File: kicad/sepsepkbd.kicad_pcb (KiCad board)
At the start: 2 copper layers, 170.7 x 127.7 mm, 53 parts, among them J1 MJ-4PP-9, J2 MJ-4PP-9, J3 Conn_01x10_Pin, J4 Conn_01x10_Pin, J5 Conn_01x10_Pin, J6 Conn_01x08_Pin, J7 Conn_01x08_Pin, SW1 SW_PUSH, SW10 SW_PUSH, SW11 SW_PUSH, SW12 SW_PUSH, SW13 SW_PUSH, SW14 SW_PUSH, SW15 SW_PUSH, SW16 SW_PUSH, SW17 SW_PUSH, SW18 SW_PUSH, SW19 SW_PUSH, SW2 SW_PUSH, SW20 SW_PUSH, SW21 SW_PUSH, SW22 SW_PUSH, SW3 SW_PUSH, SW4 SW_PUSH, SW5 SW_PUSH, SW6 SW_PUSH, SW7 SW_PUSH, SW8 SW_PUSH, SW9 SW_PUSH, U1 RP2040-Zero, U2 RP2040-Zero

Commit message: 2.03
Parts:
- moved J2 32.3 mm to (84.4, 92.0), turned to 0 degrees
- moved J1 32.1 mm to (179.2, 92.0), turned to 0 degrees
- moved J7 27.4 mm to (90.5, 124.0), turned to 45 degrees
- moved J6 27.3 mm to (173.1, 124.0), turned to -45 degrees
- moved J5 22.0 mm to (166.6, 93.9), turned to -90 degrees
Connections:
- J1 pad B: data -> u1_data
- J2 pad B: data -> u2_data
- U1 pad 0: data -> u1_data
- U2 pad 0: data -> u2_data
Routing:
- net data: track 152.2 -> 0.00 mm
- net bu2_row0: track 62.5 -> 96.5 mm, vias 2 -> 1
- net bu1_row3: track 84.7 -> 113.6 mm
- net bu2_row1: track 67.3 -> 95.9 mm, vias 2 -> 1
- net bu2_row2: track 71.9 -> 95.5 mm, vias 2 -> 1
- net bu2_5v: track 7.19 -> 30.3 mm, vias 0 -> 1
- net u2_data: track 0.00 -> 19.7 mm
- net bu1_col5: track 140.0 -> 120.3 mm, vias 3 -> 2
- net bu2_op5: track 10.7 -> 29.7 mm, vias 0 -> 1
- net bu1_5v: track 23.5 -> 40.4 mm, vias 0 -> 1
- net bu1_col6: track 138.3 -> 123.5 mm, vias 2 -> 3
- net Net-(D20-A): track 48.4 -> 59.5 mm, vias 2 -> 0
- net bu2_op4: track 14.3 -> 25.3 mm, vias 0 -> 1
- net bu2_op1: track 25.1 -> 16.3 mm, vias 0 -> 1
- net u1_data: track 0.00 -> 8.59 mm
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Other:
- board size 170.7 x 127.7 mm -> 170.8 x 130.5 mm
- board text added: "JLCJLCJLCJLC"
- board text added: "YUBINO HARA"
- board text added: "yubino hara"

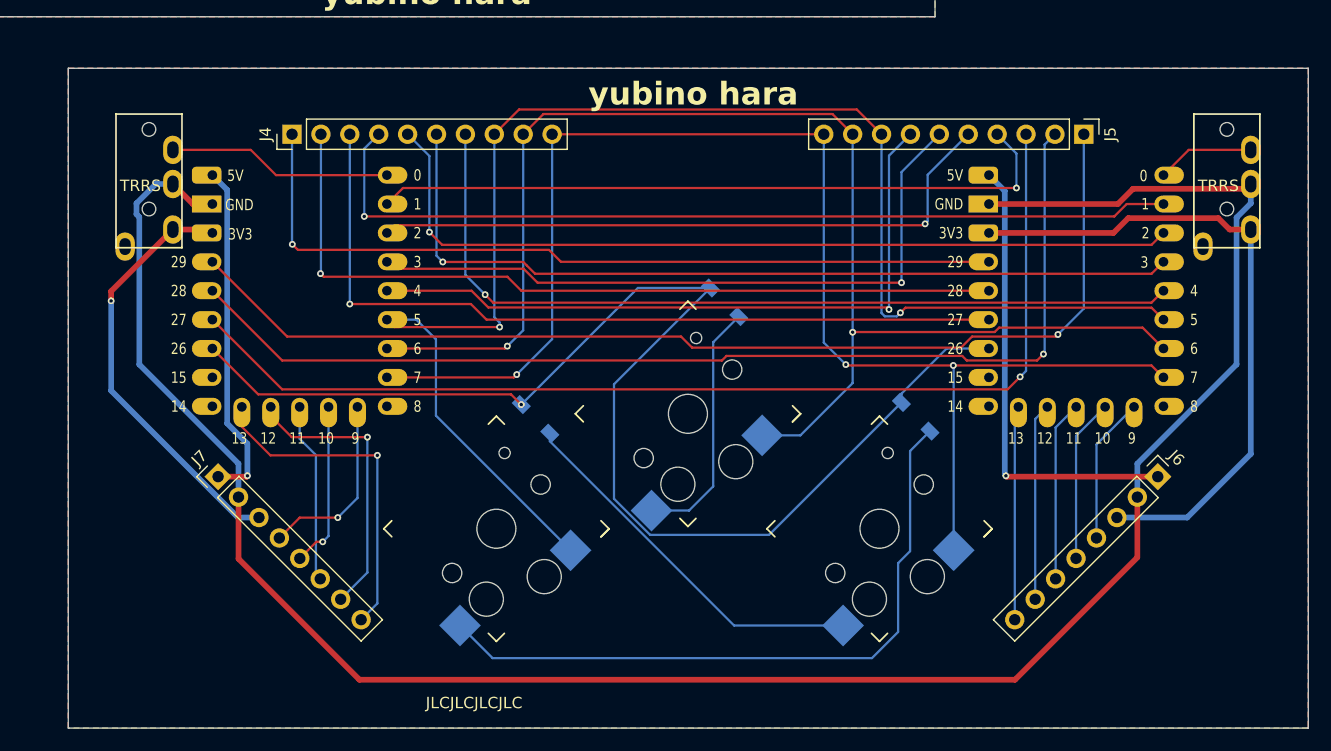
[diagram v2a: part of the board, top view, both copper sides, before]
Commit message: move trrs to the edge
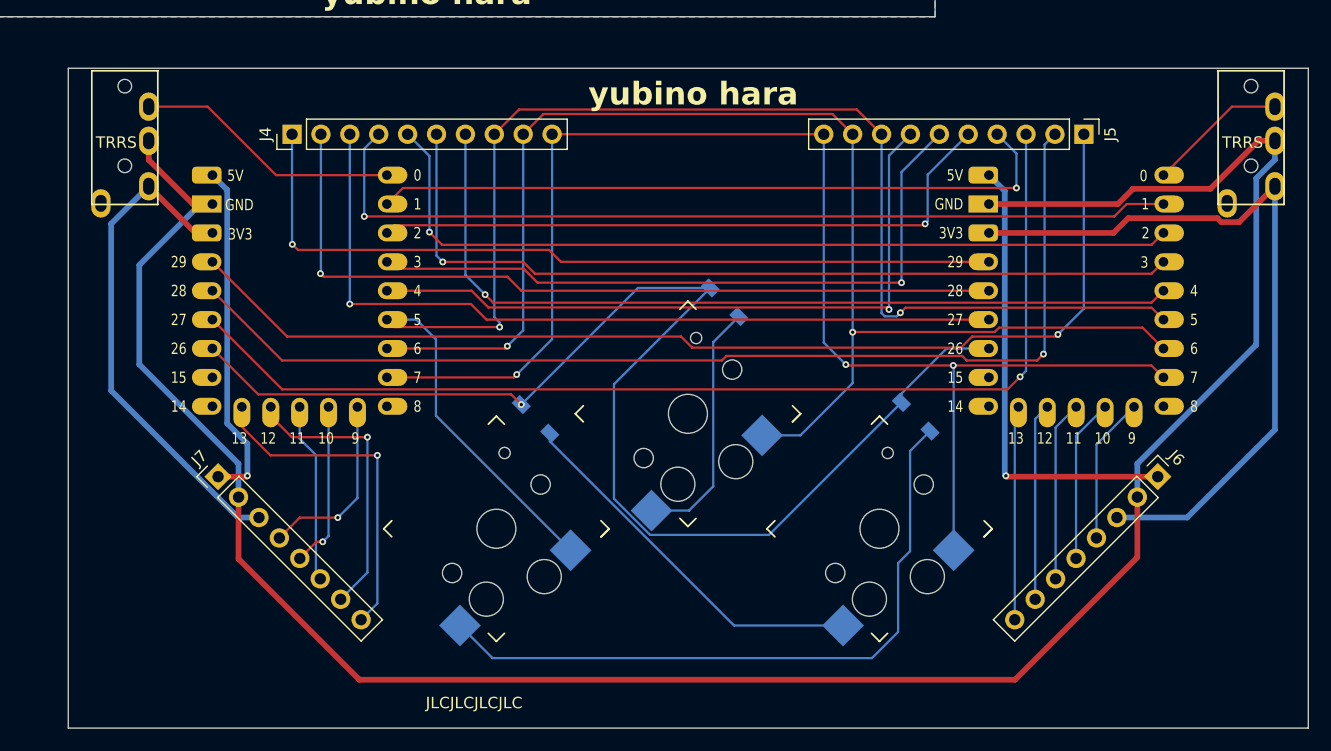
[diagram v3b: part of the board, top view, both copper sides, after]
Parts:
- moved J1 4.35 mm to (181.3, 88.2)
- moved J2 4.35 mm to (82.3, 88.2)
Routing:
- net GND: track 191.6 -> 203.9 mm
- net u1_3.3v: track 57.8 -> 65.6 mm
- net u2_3.3v: track 37.6 -> 44.7 mm, vias 1 -> 0
- net u2_data: track 19.7 -> 23.4 mm
- net u1_data: track 8.59 -> 12.3 mm
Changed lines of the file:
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@@
 	(footprint "kbd:MJ-4PP-9_1side"
 		(layer "F.Cu")
-		(at 179.175 92)
+		(at 181.3 88.2)
 		(property "Reference" "J1"
 			(at -0.85 4.95 0)
@@
 	(footprint "kbd:MJ-4PP-9_1side"
 		(layer "F.Cu")
-		(at 84.425 92)
+		(at 82.3 88.2)
 		(property "Reference" "J2"
 			(at -0.85 4.95 0)
@@
 	)
 	(gr_rect
+		(start 82.3 94.6)
+		(end 131.8 105.029616)
+		(stroke
+			(width 0.1)
+			(type default)
+		)
+		(fill none)
+		(layer "User.8")
+	)
+	(gr_rect
 		(start 81.33 92.125)
 		(end 182.33 142.125)
@@
 	(segment
 		(start 173.6 97.52)
-		(end 175.82 95.3)
+		(end 179.62 91.5)
 		(width 0.2)
 		(layer "F.Cu")
@@
 	)
 	(segment
-		(start 175.82 95.3)
-		(end 181.275 95.3)
+		(start 179.62 91.5)
+		(end 183.4 91.5)
 		(width 0.2)
 		(layer "F.Cu")
@@
 	)
 	(segment
-		(start 181.275 98.3)
-		(end 180.855 98.72)
+		(start 169.59 100.06)
+		(end 158.26 100.06)
 		(width 0.5)
 		(layer "F.Cu")
@@
 	)
 	(segment
-		(start 169.59 100.06)
-		(end 158.26 100.06)
+		(start 170.93 98.72)
+		(end 169.59 100.06)
 		(width 0.5)
 		(layer "F.Cu")
@@
 	)
 	(segment
-		(start 170.93 98.72)
-		(end 169.59 100.06)
+		(start 84.4 96.175)
+		(end 84.4 94.5)
 		(width 0.5)
 		(layer "F.Cu")
@@
 	)
 	(segment
-		(start 86.525 98.3)
-		(end 88.285 100.06)
+		(start 171.303949 131.121051)
+		(end 160.55 141.875)
 		(width 0.5)
 		(layer "F.Cu")
@@
 	)
 	(segment
-		(start 180.855 98.72)
-		(end 170.93 98.72)
+		(start 160.55 141.875)
+		(end 102.925 141.875)
 		(width 0.5)
 		(layer "F.Cu")
@@
 	)
 	(segment
-		(start 171.303949 131.121051)
-		(end 160.55 141.875)
+		(start 170.93 98.72)
+		(end 177.724365 98.72)
 		(width 0.5)
 		(layer "F.Cu")
@@
 	)
 	(segment
-		(start 160.55 141.875)
-		(end 102.925 141.875)
+		(start 177.724365 98.72)
+		(end 181.944365 94.5)
+		(width 0.5)
+		(layer "F.Cu")
+		(net 24)
+	)
+	(segment
+		(start 181.944365 94.5)
+		(end 183.4 94.5)
 		(width 0.5)
 		(layer "F.Cu")
@@
 	)
 	(segment
-		(start 92.296051 131.246051)
-		(end 92.296051 125.821051)
+		(start 88.285 100.06)
+		(end 84.4 96.175)
 		(width 0.5)
 		(layer "F.Cu")
@@
 	)
 	(segment
-		(start 171.303949 125.821051)
-		(end 171.303949 122.883107)
-		(width 0.5)
-		(layer "B.Cu")
-		(net 24)
-	)
-	(segment
-		(start 92.296051 125.821051)
-		(end 92.296051 122.883107)
+		(start 92.296051 131.246051)
+		(end 92.296051 125.821051)
 		(width 0.5)
-		(layer "B.Cu")
+		(layer "F.Cu")
 		(net 24)
 	)
 	(segment
-		(start 92.296051 122.883107)
-		(end 83.575 114.162056)
+		(start 171.303949 125.821051)
+		(end 171.303949 122.883107)
 		(width 0.5)
 		(layer "B.Cu")
@@
 	)
 	(segment
-		(start 180.025 101.25)
-		(end 181.275 100)
+		(start 183.4 96.155635)
+		(end 183.4 94.5)
 		(width 0.5)
 		(layer "B.Cu")
@@
 	)
 	(segment
-		(start 171.303949 122.883107)
-		(end 180.025 114.162056)
+		(start 92.296051 125.821051)
+		(end 92.296051 122.883107)
 		(width 0.5)
 		(layer "B.Cu")
@@
 	)
 	(segment
-		(start 83.575 101.205635)
-		(end 83.325 100.955635)
+		(start 92.296051 122.883107)
+		(end 83.575 114.162056)
 		(width 0.5)
 		(layer "B.Cu")
@@
 	)
 	(segment
-		(start 85.025 98.3)
-		(end 86.525 98.3)
+		(start 88.94 100.06)
+		(end 90 100.06)
 		(width 0.5)
 		(layer "B.Cu")
@@
 	)
 	(segment
-		(start 181.275 100)
-		(end 181.275 98.3)
+		(start 83.575 105.425)
+		(end 88.94 100.06)
 		(width 0.5)
 		(layer "B.Cu")
@@
 	)
 	(segment
-		(start 180.025 114.162056)
-		(end 180.025 101.25)
+		(start 181.755635 112.431421)
+		(end 181.755635 97.8)
 		(width 0.5)
 		(layer "B.Cu")
@@
 	)
 	(segment
-		(start 83.325 100.955635)
-		(end 83.325 100)
+		(start 181.755635 97.8)
+		(end 183.4 96.155635)
 		(width 0.5)
 		(layer "B.Cu")
@@
 	)
 	(segment
-		(start 83.325 100)
-		(end 85.025 98.3)
+		(start 83.575 114.162056)
+		(end 83.575 105.425)
 		(width 0.5)
 		(layer "B.Cu")
@@
 	)
 	(segment
-		(start 83.575 114.162056)
-		(end 83.575 101.205635)
+		(start 171.303949 122.883107)
+		(end 181.755635 112.431421)
 		(width 0.5)
 		(layer "B.Cu")
@@
 	)
 	(segment
-		(start 81.1 107.725)
-		(end 86.525 102.3)
+		(start 88.5 102.6)
+		(end 84.4 98.5)
 		(width 0.5)
 		(layer "F.Cu")
@@
 	)
 	(segment
-		(start 81.1 108.575)
-		(end 81.1 107.725)
+		(start 89.7 102.3)
+		(end 90 102.6)
 		(width 0.5)
 		(layer "F.Cu")
@@
 	)
 	(segment
-		(start 86.525 102.3)
-		(end 89.7 102.3)
+		(start 90 102.6)
+		(end 88.5 102.6)
 		(width 0.5)
 		(layer "F.Cu")
@@
 	)
 	(segment
-		(start 89.7 102.3)
-		(end 90 102.6)
+		(start 92.253624 127.617102)
+		(end 81.1 116.463478)
 		(width 0.5)
-		(layer "F.Cu")
-		(net 35)
-	)
-	(via
-		(at 81.1 108.575)
-		(size 0.6)
-		(drill 0.3)
-		(layers "F.Cu" "B.Cu")
+		(layer "B.Cu")
 		(net 35)
 	)
 	(segment
-		(start 92.253624 127.617102)
-		(end 81.1 116.463478)
+		(start 81.1 101.8)
+		(end 84.4 98.5)
 		(width 0.5)
 		(layer "B.Cu")
@@
 	)
 	(segment
-		(start 94.092102 127.617102)
-		(end 92.253624 127.617102)
+		(start 81.1 116.463478)
+		(end 81.1 101.8)
 		(width 0.5)
 		(layer "B.Cu")
@@
 	)
 	(segment
-		(start 81.1 116.463478)
-		(end 81.1 108.575)
+		(start 94.092102 127.617102)
+		(end 92.253624 127.617102)
 		(width 0.5)
 		(layer "B.Cu")
@@
 	)
 	(segment
-		(start 178.419365 101.3)
-		(end 170.5 101.3)
+		(start 170.5 101.3)
+		(end 178.332233 101.3)
 		(width 0.5)
 		(layer "F.Cu")
@@
 	)
 	(segment
-		(start 179.419365 102.3)
-		(end 178.419365 101.3)
+		(start 178.332233 101.3)
+		(end 178.682233 101.65)
 		(width 0.5)
 		(layer "F.Cu")
@@
 	)
 	(segment
-		(start 181.275 102.3)
-		(end 179.419365 102.3)
+		(start 178.682233 101.65)
+		(end 180.25 101.65)
 		(width 0.5)
 		(layer "F.Cu")
@@
 	)
 	(segment
-		(start 181.275 122.025)
-		(end 175.682898 127.617102)
+		(start 180.25 101.65)
+		(end 183.4 98.5)
+		(width 0.5)
+		(layer "F.Cu")
+		(net 43)
+	)
+	(segment
+		(start 175.682898 127.617102)
+		(end 183.4 119.9)
 		(width 0.5)
 		(layer "B.Cu")
@@
 	)
 	(segment
-		(start 181.275 102.3)
-		(end 181.275 122.025)
+		(start 183.4 119.9)
+		(end 183.4 98.5)
 		(width 0.5)
 		(layer "B.Cu")
@@
 	)
 	(segment
-		(start 86.525 95.3)
-		(end 93.375 95.3)
+		(start 95.595 97.52)
+		(end 89.575 91.5)
 		(width 0.2)
 		(layer "F.Cu")
@@
 	)
 	(segment
-		(start 93.375 95.3)
-		(end 95.595 97.52)
+		(start 89.575 91.5)
+		(end 84.4 91.5)
 		(width 0.2)
 		(layer "F.Cu")
@@
 	)
 	(segment
-		(start 95.595 97.52)
-		(end 105.34 97.52)
+		(start 105.34 97.52)
+		(end 95.595 97.52)
 		(width 0.2)
 		(layer "F.Cu")
@@
 			)
 		)
-	)
-	(zone
-		(net 24)
-		(net_name "GND")
-		(layers "F&B.Cu")
-		(hatch edge 0.5)
-		(priority 1)
-		(connect_pads
-			(clearance 0.5)
-		)
-		(min_thickness 0.25)
-		(filled_areas_thickness no)
-		(fill yes
-			(thermal_gap 0.5)
-			(thermal_bridge_width 0.5)
-		)
-		(polygon
-			(pts
-				(xy 77.33 88.125) (xy 186.33 88.125) (xy 186.33 146.125) (xy 77.33 146.125)
-			)
-		)

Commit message: 2.04
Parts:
- moved D19 5.71 mm to (137.2, 60.5), turned to -90 degrees
- moved SW19 1.50 mm to (144.2, 56.0)
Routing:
- net Net-(D19-A): track 10.8 -> 24.9 mm
- net /t_col6: track 34.9 -> 32.9 mm
- net /t_row2: track 127.9 -> 127.1 mm, vias 7 -> 6
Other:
- outline, holes or cut-outs redrawn

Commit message: tmp
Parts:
- SW19: footprint kbd:ResetSW -> keyswitches:Kailh_socket_PG1350_reversible
- moved J1 31.9 mm to (151.8, 100.1), turned to -45 degrees
- moved U1 4.02 mm to (165.8, 111.7), turned to -45 degrees
- moved SW19 3.94 mm to (148.1, 55.7)
- moved D19 0.28 mm to (136.9, 60.5)
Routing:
- net u1_data: track 12.3 -> 0.00 mm
- net GND: track 203.9 -> 216.2 mm
- net /t_col6: track 32.9 -> 42.7 mm, vias 0 -> 1
- net Net-(D19-A): track 24.9 -> 34.1 mm, vias 0 -> 2
- net /t_row2: track 127.1 -> 126.5 mm
- removed copper zone on B.Cu, net GND
- removed copper zone on F.Cu, net GND
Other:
- board size 170.8 x 130.5 mm -> 166.9 x 128.5 mm
- board text added: "HIDARI YON-HON YUBI"
- board text added: "MIGI YON-HON YUBI"
- board text added: "OYA YUBI"
- board text added: "Yubino Hara"
- board text removed: "YUBINO HARA"
- board text removed: "yubino hara"

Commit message: Four-finger boards reduced to the bare minimum
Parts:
- moved J1 31.8 mm to (181.3, 88.3), turned to 0 degrees
- moved U1 4.02 mm to (165.9, 107.7), turned to 0 degrees
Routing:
- net u1_data: track 0.00 -> 12.3 mm
- net GND: track 216.2 -> 203.9 mm
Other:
- board text added: "OYAYUBI"
- board text removed: "OYA YUBI"

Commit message: Split thumbsboard left and right.
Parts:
- removed the D1 at (38.4, 22.5)
- removed the D2 at (57.4, 22.5)
- removed the D3 at (76.4, 22.5)
- removed J7: Conn_01x08_Pin, Connector_PinHeader_2.54mm:PinHeader_1x08_P2.54mm_Vertical
- removed the SW1 at (29.0, 27.1)
- removed the SW2 at (48.1, 27.1)
- removed the SW3 at (67.1, 27.1)
- added D20: D, kbd:D3_SMD, F.Cu at (119.4, 41.5)
- added D21: D, kbd:D3_SMD, F.Cu at (114.4, 60.5)
- added D22: D, kbd:D3_SMD, F.Cu at (133.4, 22.5)
- added D23: D, kbd:D3_SMD, F.Cu at (138.4, 41.5)
- added D24: D, kbd:D3_SMD, F.Cu at (133.9, 60.5)
- added D25: D, kbd:D3_SMD, F.Cu at (136.9, 60.5)
- added J9: Conn_01x10_Pin, Connector_PinHeader_2.54mm:PinHeader_1x10_P2.54mm_Vertical, F.Cu at (97.0, 78.0)
- added REF**: ThumbsBoard_logo, sepsepkbd:ThumbsBoard_logo, F.Cu at (48.7, 129.4)
- added REF**: 4FingerBoard_logo, sepsepkbd:4FingerBoard_logo, F.Cu at (145.2, 25.1)
- added REF**: ThumbsBoard_logo, sepsepkbd:ThumbsBoard_logo, F.Cu at (150.2, 129.4)
- added SW20: SW_PUSH, keyswitches:Kailh_socket_PG1350_reversible, F.Cu at (110.0, 46.1)
- added SW21: SW_PUSH, keyswitches:Kailh_socket_PG1350_reversible, F.Cu at (105.2, 65.2)
- added SW22: SW_PUSH, keyswitches:Kailh_socket_PG1350_reversible, F.Cu at (124.3, 27.1)
- added SW23: SW_PUSH, keyswitches:Kailh_socket_PG1350_reversible, F.Cu at (129.0, 46.1)
- added SW24: SW_PUSH, keyswitches:Kailh_socket_PG1350_reversible, F.Cu at (124.3, 65.2)
- added SW25: SW_PUSH, keyswitches:Kailh_socket_PG1350_reversible, F.Cu at (148.1, 55.7)
- D4, D5, D6: footprint kbd:D3_SMD -> kbd:D3_SMD_v2; moved to B.Cu
- J3: value Conn_01x10_Pin -> Conn_01x08_Pin; footprint Connector_PinHeader_2.54mm:PinHeader_1x10_P2.54mm_Vertical -> Connector_PinHeader_2.54mm:PinHeader_1x08_P2.54mm_Vertical
- SW4, SW5, SW6: footprint keyswitches:Kailh_socket_PG1350_reversible -> keyswitches:Kailh_socket_PG1350
- moved J6 137.9 mm to (39.2, 91.0), turned to -90 degrees
- moved D6 115.8 mm to (46.7, 99.2), turned to -135 degrees
- moved D4 108.8 mm to (29.9, 109.3), turned to -135 degrees
- moved SW6 108.6 mm to (66.7, 119.2), turned to -45 degrees
- moved SW4 106.3 mm to (33.1, 119.2), turned to -45 degrees
- moved D5 100.9 mm to (63.3, 109.5), turned to -135 degrees
- moved SW5 98.9 mm to (49.9, 109.0), turned to -45 degrees
- moved D12 83.2 mm to (57.4, 60.5)
- moved SW12 83.2 mm to (48.1, 65.2)
- moved J4 82.4 mm to (84.7, 84.5)
- moved J3 66.3 mm to (162.0, 91.1)
- moved SW11 57.1 mm to (52.8, 46.1)
- moved D11 57.0 mm to (62.4, 41.5)
- moved SW13 53.9 mm to (67.1, 27.1)
- moved D13 53.7 mm to (76.4, 22.5)
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- renumbered D20 to D1, D21 to D2, D22 to D3, J4 to J1, J1 to J2, J5 to J4, J2 to J5, SW20 to SW1, SW21 to SW2, SW22 to SW3
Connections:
- D10 pad 1: /t_row1 -> /4Finger/t_row0
- D11 pad 1: /t_row1 -> /4Finger/t_row1
- D12 pad 1: /t_row1 -> /4Finger/t_row2
- D13 pad 1: /t_row2 -> /4Finger/t_row0
- D14 pad 1: /t_row2 -> /4Finger/t_row1
- D15 pad 1: /t_row2 -> /4Finger/t_row2
- D16 pad 1: /t_row2 -> /4Finger/t_row0
- D17 pad 1: /t_row2 -> /4Finger/t_row1
- D18 pad 1: /t_row2 -> /4Finger/t_row2
- D19 pad 1: /t_row2 -> /4Finger/t_row0
- D4 pad 1: /t_row0 -> bu2_row3
- D5 pad 1: /t_row0 -> bu2_row3
- D6 pad 1: /t_row0 -> bu2_row3
- D7 pad 1: /t_row1 -> /4Finger/t_row0
- D8 pad 1: /t_row1 -> /4Finger/t_row1
- D9 pad 1: /t_row1 -> /4Finger/t_row2
- J3 pad 1: /t_row0 -> bu1_5v
- J3 pad 2: /t_row1 -> GND
- J3 pad 3: /t_row2 -> u1_3.3v
- J3 pad 4: /t_col0 -> bu1_op1
- J3 pad 5: /t_col1 -> bu1_op2
- J3 pad 6: /t_col2 -> bu1_op3
- J3 pad 7: /t_col3 -> bu1_op4
- J3 pad 8: /t_col4 -> bu1_op5
- J4 pad 10: bu1_col6 -> bu2_col6
- J4 pad 8: bu1_col4 -> bu2_col4
- J4 pad 9: bu1_col5 -> bu2_col5
- J6 pad 1: bu1_5v -> bu2_5v
- J6 pad 3: u1_3.3v -> u2_3.3v
- J6 pad 4: bu1_op1 -> bu2_op1
- J6 pad 5: bu1_op2 -> bu2_op2
- J6 pad 6: bu1_op3 -> bu2_op3
- J6 pad 7: bu1_op4 -> bu2_op4
- J6 pad 8: bu1_op5 -> bu2_op5
- SW10 pad 1: /t_col3 -> /4Finger/t_col1
- SW11 pad 1: /t_col4 -> /4Finger/t_col1
- SW12 pad 1: /t_col5 -> /4Finger/t_col1
- SW13 pad 1: /t_col0 -> /4Finger/t_col2
- SW14 pad 1: /t_col1 -> /4Finger/t_col2
- SW15 pad 1: /t_col2 -> /4Finger/t_col2
- SW16 pad 1: /t_col3 -> /4Finger/t_col3
- SW17 pad 1: /t_col4 -> /4Finger/t_col3
- SW18 pad 1: /t_col5 -> /4Finger/t_col3
- SW19 pad 1: /t_col6 -> /4Finger/t_col4
- SW4 pad 1: /t_col3 -> bu2_col4
- SW5 pad 1: /t_col4 -> bu2_col5
- SW6 pad 1: /t_col5 -> bu2_col6
- SW7 pad 1: /t_col0 -> /4Finger/t_col0
- SW8 pad 1: /t_col1 -> /4Finger/t_col0
- SW9 pad 1: /t_col2 -> /4Finger/t_col0
- U2 pad 26: bu1_row3 -> bu2_row3
- U2 pad 5: bu1_col4 -> bu2_col4
- U2 pad 6: bu1_col5 -> bu2_col5
- U2 pad 7: bu1_col6 -> bu2_col6
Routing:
- net /t_row0: track 263.0 -> 0.00 mm, vias 1 -> 0
- net /4Finger/t_row0: track 0.00 -> 263.0 mm, vias 0 -> 1
- net GND: track 203.9 -> 0.00 mm
- net /t_col0: track 144.3 -> 0.00 mm, vias 3 -> 0
- net /4Finger/t_col0: track 0.00 -> 144.3 mm, vias 0 -> 3
- net /t_row1: track 143.5 -> 0.00 mm, vias 6 -> 0
- net /4Finger/t_row1: track 0.00 -> 143.5 mm, vias 0 -> 6
- net bu1_col4: track 133.0 -> 0.00 mm, vias 2 -> 0
- net /t_col1: track 131.7 -> 0.00 mm, vias 3 -> 0
- net /4Finger/t_col1: track 0.00 -> 131.7 mm, vias 0 -> 3
- net /t_row2: track 126.5 -> 0.00 mm, vias 6 -> 0
- net /4Finger/t_row2: track 0.00 -> 126.5 mm, vias 0 -> 6
- net bu1_col6: track 123.5 -> 0.00 mm, vias 3 -> 0
- net bu1_col5: track 120.3 -> 0.00 mm, vias 2 -> 0
- net /t_col2: track 115.3 -> 0.00 mm, vias 3 -> 0
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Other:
- board size 166.9 x 128.5 mm -> 162.2 x 115 mm
- board text added: "右"
- board text added: "左"
- board text removed: "HIDARI YON-HON YUBI"
- board text removed: "MIGI YON-HON YUBI"
- board text removed: "OYAYUBI"
- board text removed: "Yubino Hara"
